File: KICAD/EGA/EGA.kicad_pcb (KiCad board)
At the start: 2 copper layers, 37 parts, among them J1 12V, J2 HC-SR04, J3 LCD 20x4, J4 RTC, J6 FAN_12V_PWM_3.3V, J7 SD CARD, SW1 PAGINA, SW2 RESET, U1 LM7805_TO220, U2 LM317_TO-220, U3 Pico

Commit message: Actualizacion de EGA en KICAD
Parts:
- removed R1: 2K, Resistor_THT:R_Axial_DIN0204_L3.6mm_D1.6mm_P7.62mm_Horizontal
- removed R2: 1K, Resistor_THT:R_Axial_DIN0204_L3.6mm_D1.6mm_P7.62mm_Horizontal
- added J10: TEST_TRIG, Connector_PinHeader_2.54mm:PinHeader_1x01_P2.54mm_Vertical, F.Cu at (103.2, 89.2)
- added J5: TEST_PWM, Connector_PinHeader_2.54mm:PinHeader_1x01_P2.54mm_Vertical, F.Cu at (140.3, 101.1)
- added J8: TEST_RPM, Connector_PinHeader_2.54mm:PinHeader_1x01_P2.54mm_Vertical, F.Cu at (140.3, 107.1)
- added J9: TEST_ECHO, Connector_PinHeader_2.54mm:PinHeader_1x01_P2.54mm_Vertical, F.Cu at (81.4, 94.5)
- moved J2 11.8 mm to (85.2, 90.9)
- moved D4 2.84 mm to (94.2, 85.3), turned to 0 degrees
- moved D5 2.79 mm to (94.1, 78.7), turned to 0 degrees
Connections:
- J2 pad 3: Net-(J2-Pin_3) -> ECHO
- J7 pad 1: GND -> unconnected-(J7-Pin_1-Pad1)
- U3 pad 13: GND -> unconnected-(U3-GND-Pad13)_0
- U3 pad 18: GND -> unconnected-(U3-GND-Pad18)_0
- U3 pad 19: ECHO -> TRIG
- U3 pad 20: TRIG -> ECHO
- U3 pad 21: PIN_PAGINA -> UART_TX
- U3 pad 22: unconnected-(U3-GPIO17-Pad22)_0 -> UART_RX
- U3 pad 23: GND -> unconnected-(U3-GND-Pad23)_0
- U3 pad 24: unconnected-(U3-GPIO18-Pad24) -> PIN_PAGINA
- U3 pad 8: GND -> unconnected-(U3-GND-Pad8)
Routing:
- net 5V: track 284.3 -> 356.2 mm
- net GND: track 478.5 -> 435.5 mm, vias 4 -> 6
- net ECHO: track 12.6 -> 39.8 mm
- net SCL_1: track 0.00 -> 16.8 mm, vias 0 -> 1
- net SDA_1: track 0.00 -> 16.8 mm, vias 0 -> 1
- net TRIG: track 22.8 -> 39.6 mm
- net UART_RX: track 0.00 -> 14.7 mm, vias 0 -> 1
- net UART_TX: track 0.00 -> 14.5 mm, vias 0 -> 1
- net PIN_RPM: track 34.6 -> 46.7 mm
- net PIN_CS: track 42.3 -> 53.7 mm
- net Net-(J2-Pin_3): track 9.11 -> 0.00 mm
- net PIN_PWM: track 38.9 -> 46.4 mm
- net PIN_PAGINA: track 33.2 -> 26.9 mm
- net PIN_SCK: track 34.1 -> 29.0 mm, vias 0 -> 2
- net Net-(D5-A): track 10.0 -> 7.87 mm
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- added copper zone on B.Cu, net GND

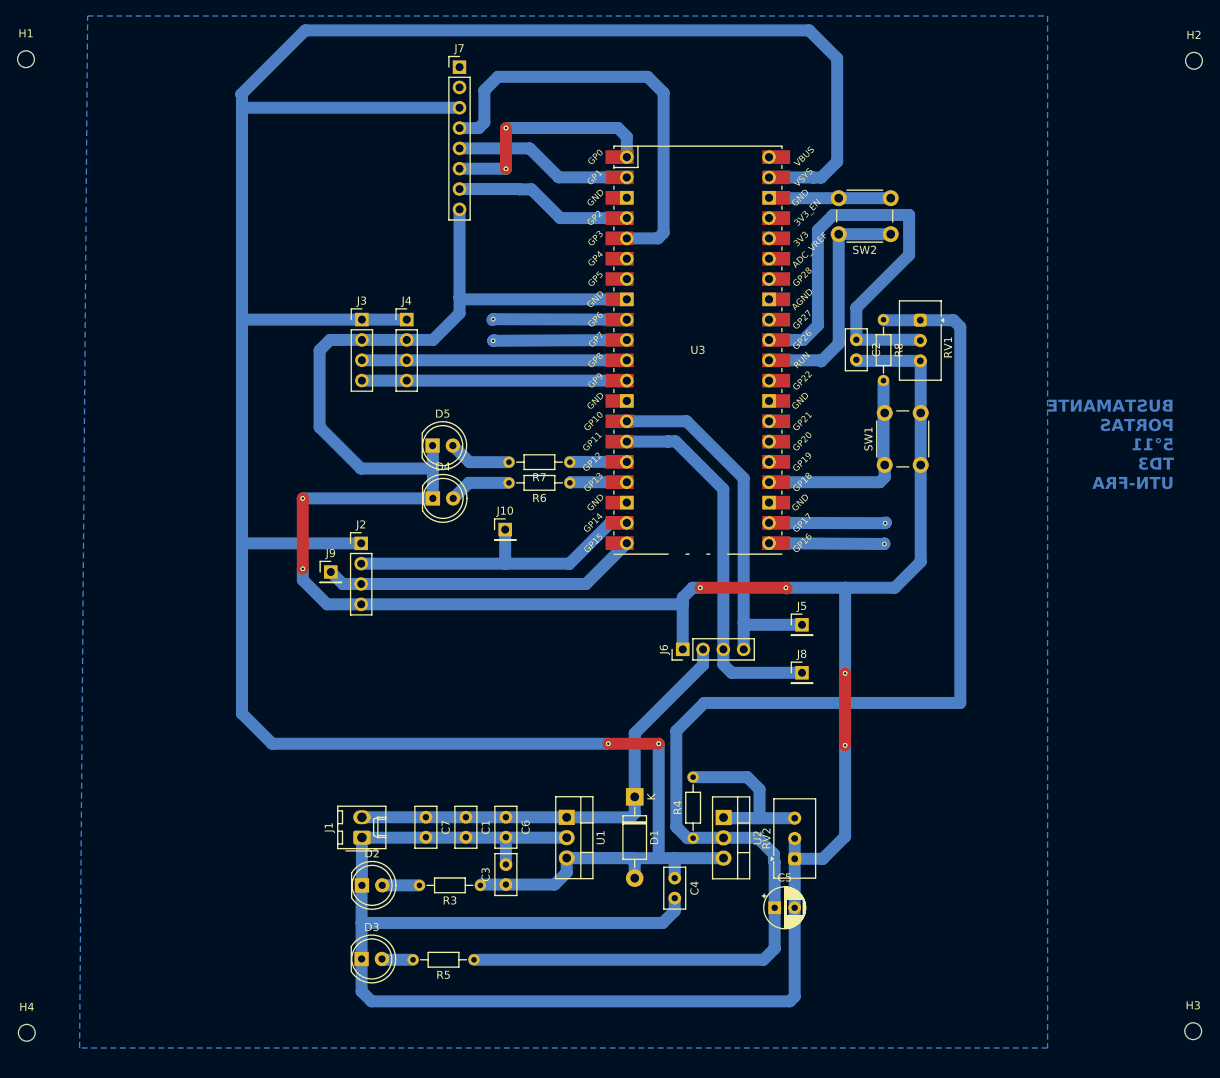
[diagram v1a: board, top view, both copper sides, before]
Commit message: Actualizacion KICAD, CAmbio de pines en UART, los pines de I2C se mantienen sin cambios
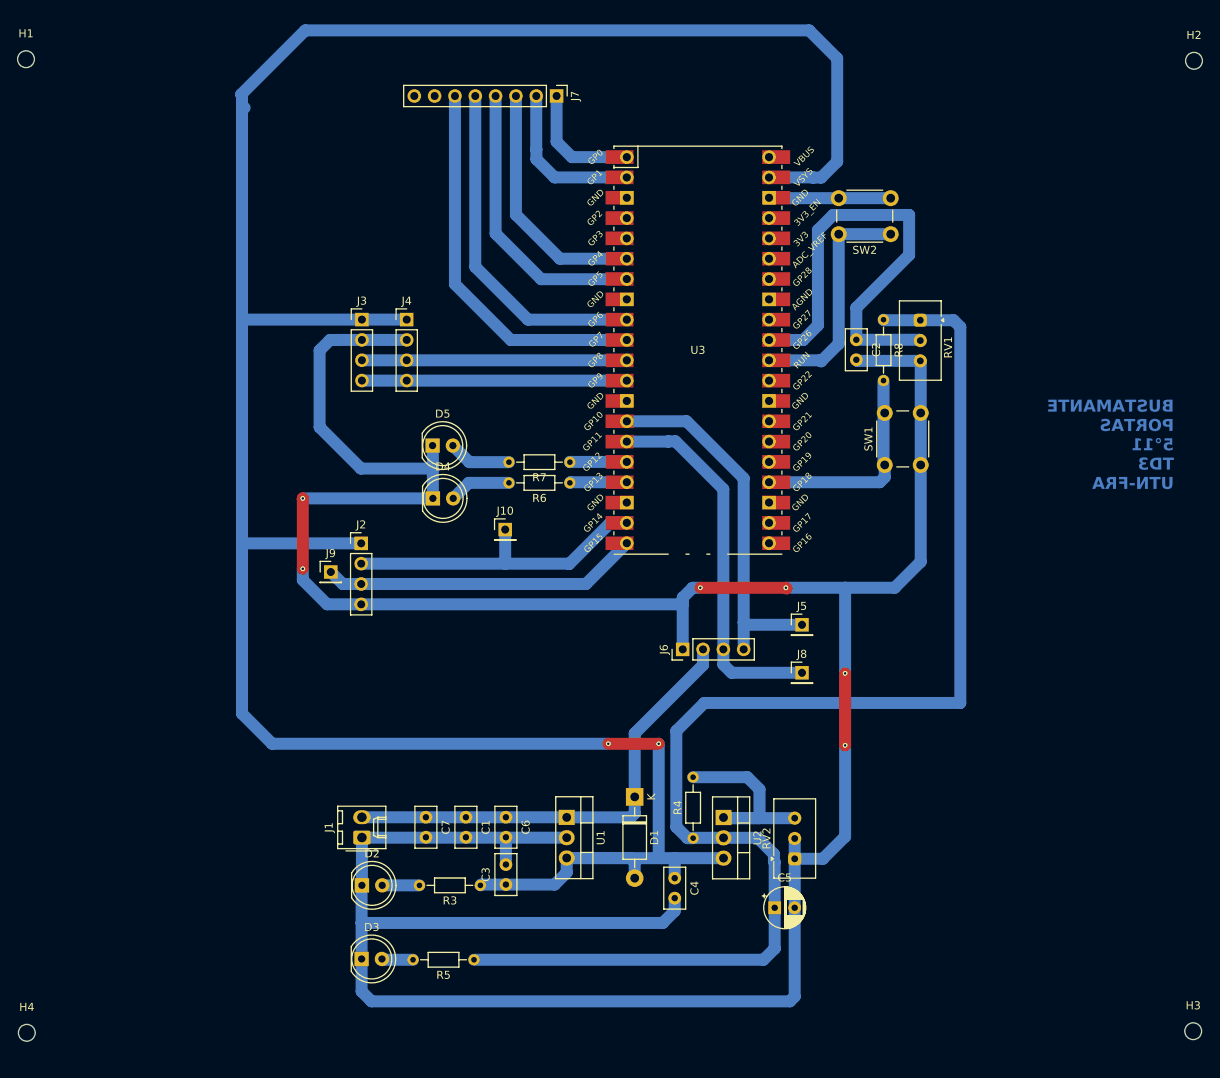
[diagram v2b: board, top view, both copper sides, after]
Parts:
- J7: value SD CARD -> UART
- moved J7 12.7 mm to (109.6, 35.0), turned to -90 degrees
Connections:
- J7 pad 1: unconnected-(J7-Pin_1-Pad1) -> UART0_TX
- J7 pad 2: unconnected-(J7-Pin_2-Pad2) -> UART0_RX
- J7 pad 3: 5V -> UART1_TX
- J7 pad 4: PIN_CS -> UART1_RX
- J7 pad 5: PIN_TX_MOSI -> SDA_1
- J7 pad 6: PIN_SCK -> SCL_1
- J7 pad 7: PIN_RX_MISO -> unconnected-(J7-Pin_7-Pad7)
- J7 pad 8: GND -> unconnected-(J7-Pin_8-Pad8)
- U3 pad 1: PIN_SCK -> UART0_TX
- U3 pad 2: PIN_TX_MOSI -> UART0_RX
- U3 pad 21: UART_TX -> unconnected-(U3-GPIO16-Pad21)
- U3 pad 22: UART_RX -> unconnected-(U3-GPIO17-Pad22)_0
- U3 pad 4: PIN_RX_MISO -> unconnected-(U3-GPIO2-Pad4)_0
- U3 pad 5: PIN_CS -> unconnected-(U3-GPIO3-Pad5)
- U3 pad 6: unconnected-(U3-GPIO4-Pad6)_0 -> UART1_TX
- U3 pad 7: unconnected-(U3-GPIO5-Pad7)_0 -> UART1_RX
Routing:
- net PIN_CS: track 53.7 -> 0.00 mm
- net GND: track 435.5 -> 393.6 mm
- net UART1_RX: track 0.00 -> 36.0 mm
- net SCL_1: track 16.8 -> 47.9 mm, vias 1 -> 0
- net UART1_TX: track 0.00 -> 31.0 mm
- net PIN_SCK: track 29.0 -> 0.00 mm, vias 2 -> 0
- net 5V: track 356.2 -> 329.3 mm
- net SDA_1: track 16.8 -> 43.0 mm, vias 1 -> 0
- net PIN_TX_MOSI: track 22.4 -> 0.00 mm
- net PIN_RX_MISO: track 22.4 -> 0.00 mm
- net UART0_RX: track 0.00 -> 20.2 mm
- net UART0_TX: track 0.00 -> 15.3 mm
- net UART_RX: track 14.7 -> 0.00 mm, vias 1 -> 0
- net UART_TX: track 14.5 -> 0.00 mm, vias 1 -> 0
- removed copper zone on B.Cu, net GND

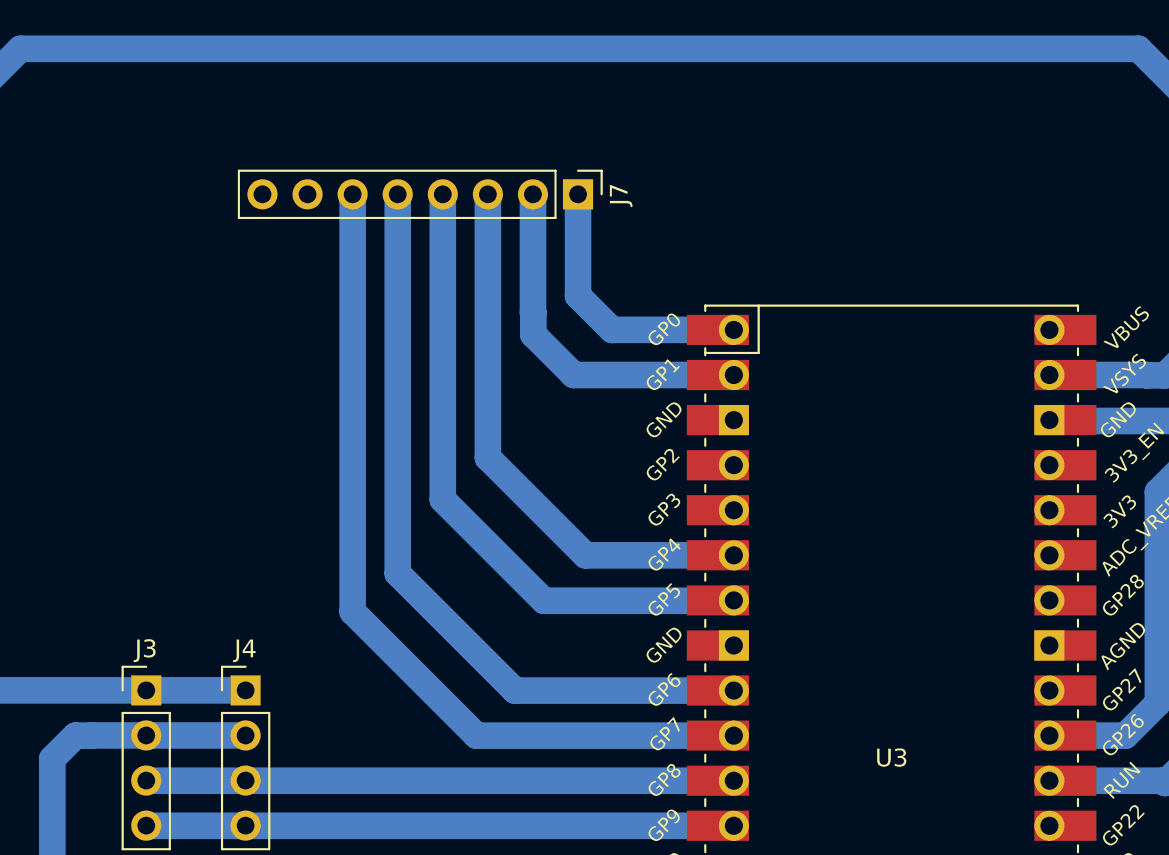
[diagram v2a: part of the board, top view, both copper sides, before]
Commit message: Cambios en Kicad, adicion de Cuentionario, Adicion de informe
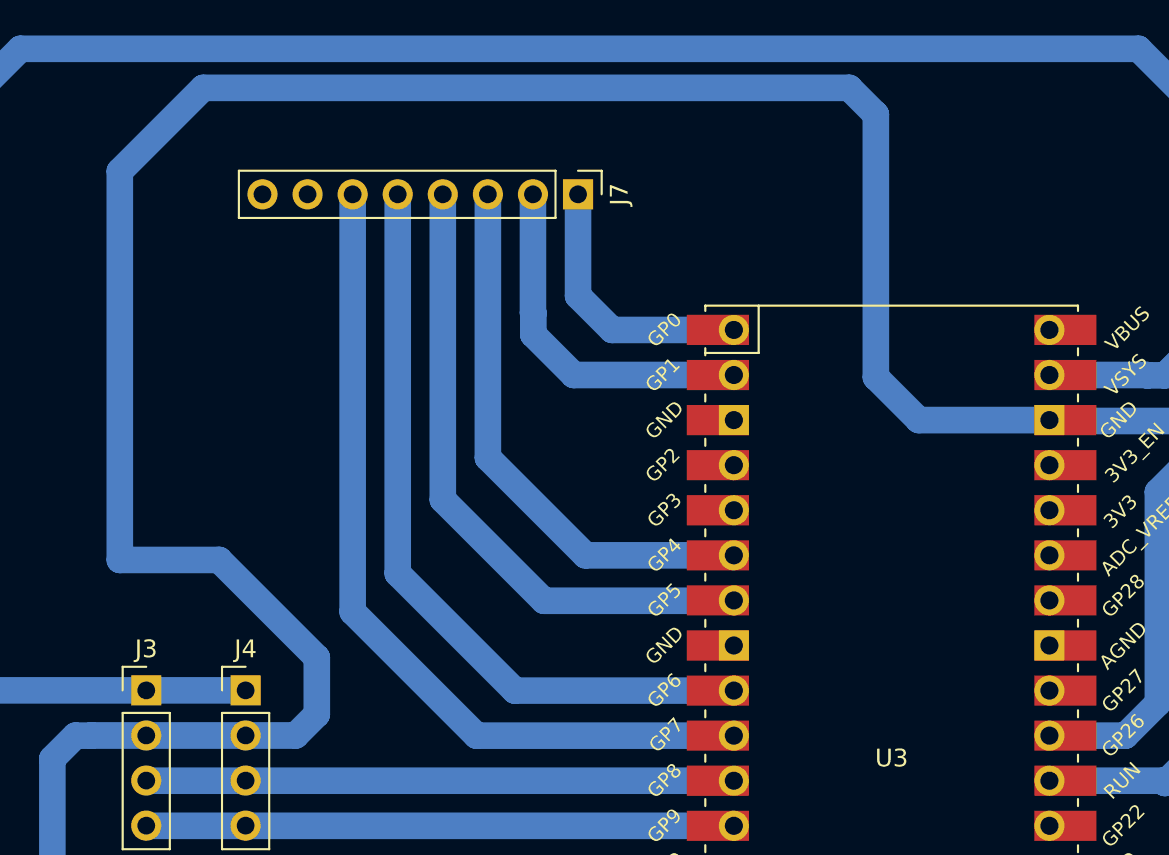
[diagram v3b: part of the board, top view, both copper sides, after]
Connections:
- SW2 pad 2: Net-(SW2-Pad2) -> GND
- U3 pad 38: Net-(SW2-Pad2) -> GND
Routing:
- net GND: track 393.6 -> 522.6 mm
- net Net-(SW2-Pad2): track 15.3 -> 0.00 mm

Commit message: Plano de masa en PCB
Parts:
- moved J9 22.1 mm to (102.9, 99.6)
- moved D2 3.65 mm to (84.9, 137.3)
- moved R3 3.65 mm to (99.7, 137.3)
- moved J5 3.65 mm to (139.9, 104.7)
- moved J8 3.65 mm to (139.9, 110.7)
- moved D4 3.65 mm to (93.8, 88.9)
- moved R4 3.65 mm to (126.3, 131.4)
- moved R7 3.65 mm to (110.9, 84.4)
- moved U1 3.65 mm to (110.5, 128.8)
- moved U3 3.65 mm to (126.9, 70.4)
- moved R8 3.65 mm to (150.1, 66.6)
- moved J7 3.65 mm to (109.2, 38.6)
- moved C2 3.65 mm to (146.7, 69.1)
- moved RV1 3.65 mm to (154.7, 66.7)
- moved U2 3.65 mm to (130.1, 128.8)
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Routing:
- net ECHO: track 39.8 -> 37.0 mm
- added copper zone on B.Cu, net GND
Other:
- board text added: "+"
- board text added: "12V"
- board text added: "3.3V"
- board text added: "5V"
- board text added: "ECHO"
- board text added: "GND"
- board text added: "MAXIMA ALTURA"
- board text added: "MINIMA ALTURA"
- board text added: "OPCION"
- board text added: "PWM"
- board text added: "RESET"
- board text added: "RPM"
- board text added: "RX0"
- board text added: "RX1"
- board text added: "SCL"
- board text added: "SCL1"
- board text added: "SDA"
- board text added: "SDA1"
- board text added: "SETPOINT"
- board text added: "TRIG"
- board text added: "TX0"
- board text added: "TX1"
- board text added: "T_ECHO"
- board text added: "T_PWM"
- board text added: "T_RPM"
- board text added: "T_TRIG"
